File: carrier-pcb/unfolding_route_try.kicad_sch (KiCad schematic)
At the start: 71 parts, among them J1 USB4125-GF-A_REVA, J2 Conn_01x01_Female, J3 1-338068-8, J4 Conn_01x01_Female, J5 Conn_01x01_Female, J6 Conn_01x01_Female, U1 TCA9548APWR, U10 DRV2605LDGS, U11 DRV2605LDGS, U12 BMX160, U13 USBLC6-2SC6, U2 TCA9548APWR, U3 DRV2605LDGS, U4 DRV2605LDGS, U5 DRV2605LDGS, U6 DRV2605LDGS, U7 DRV2605LDGS, U8 DRV2605LDGS, U9 DRV2605LDGS

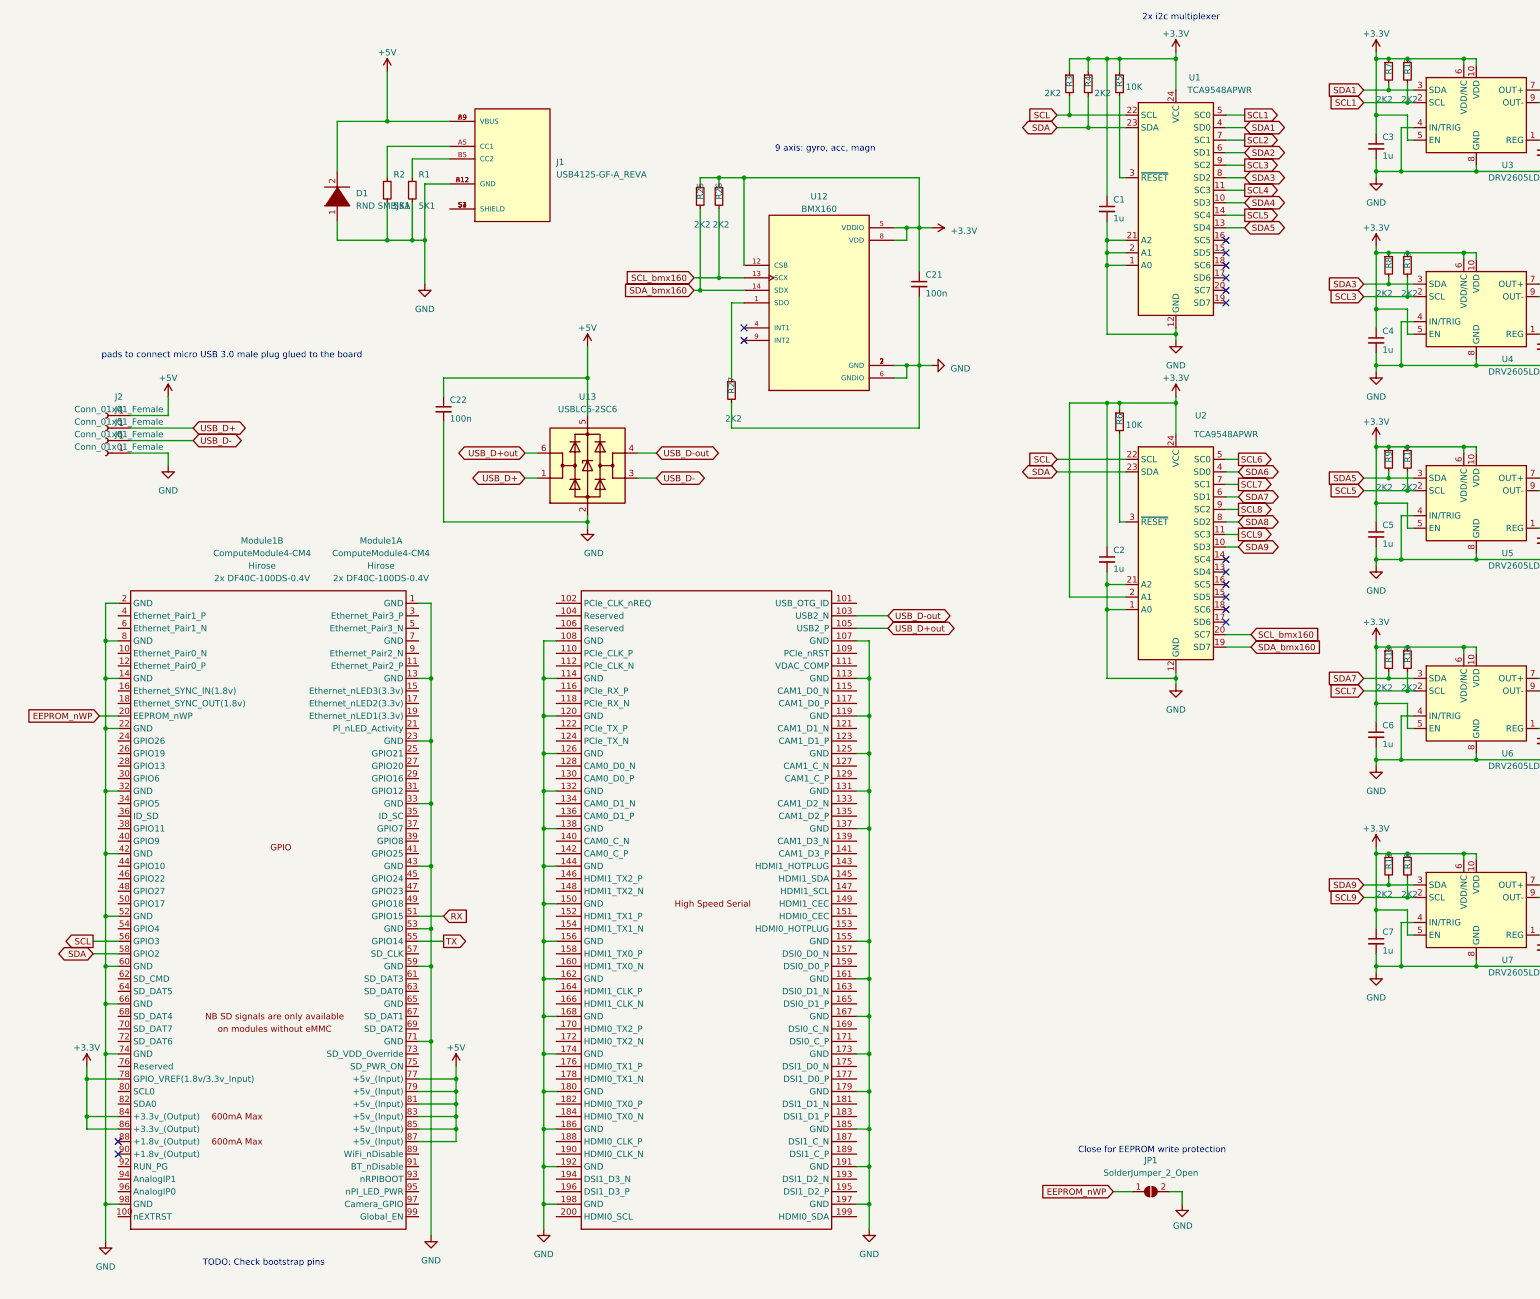
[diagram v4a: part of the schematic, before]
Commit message: Added compass, added LEDs, changed USB TVS diode, fixed power TVS diode direction, moved accelerometer, misc minor improvements
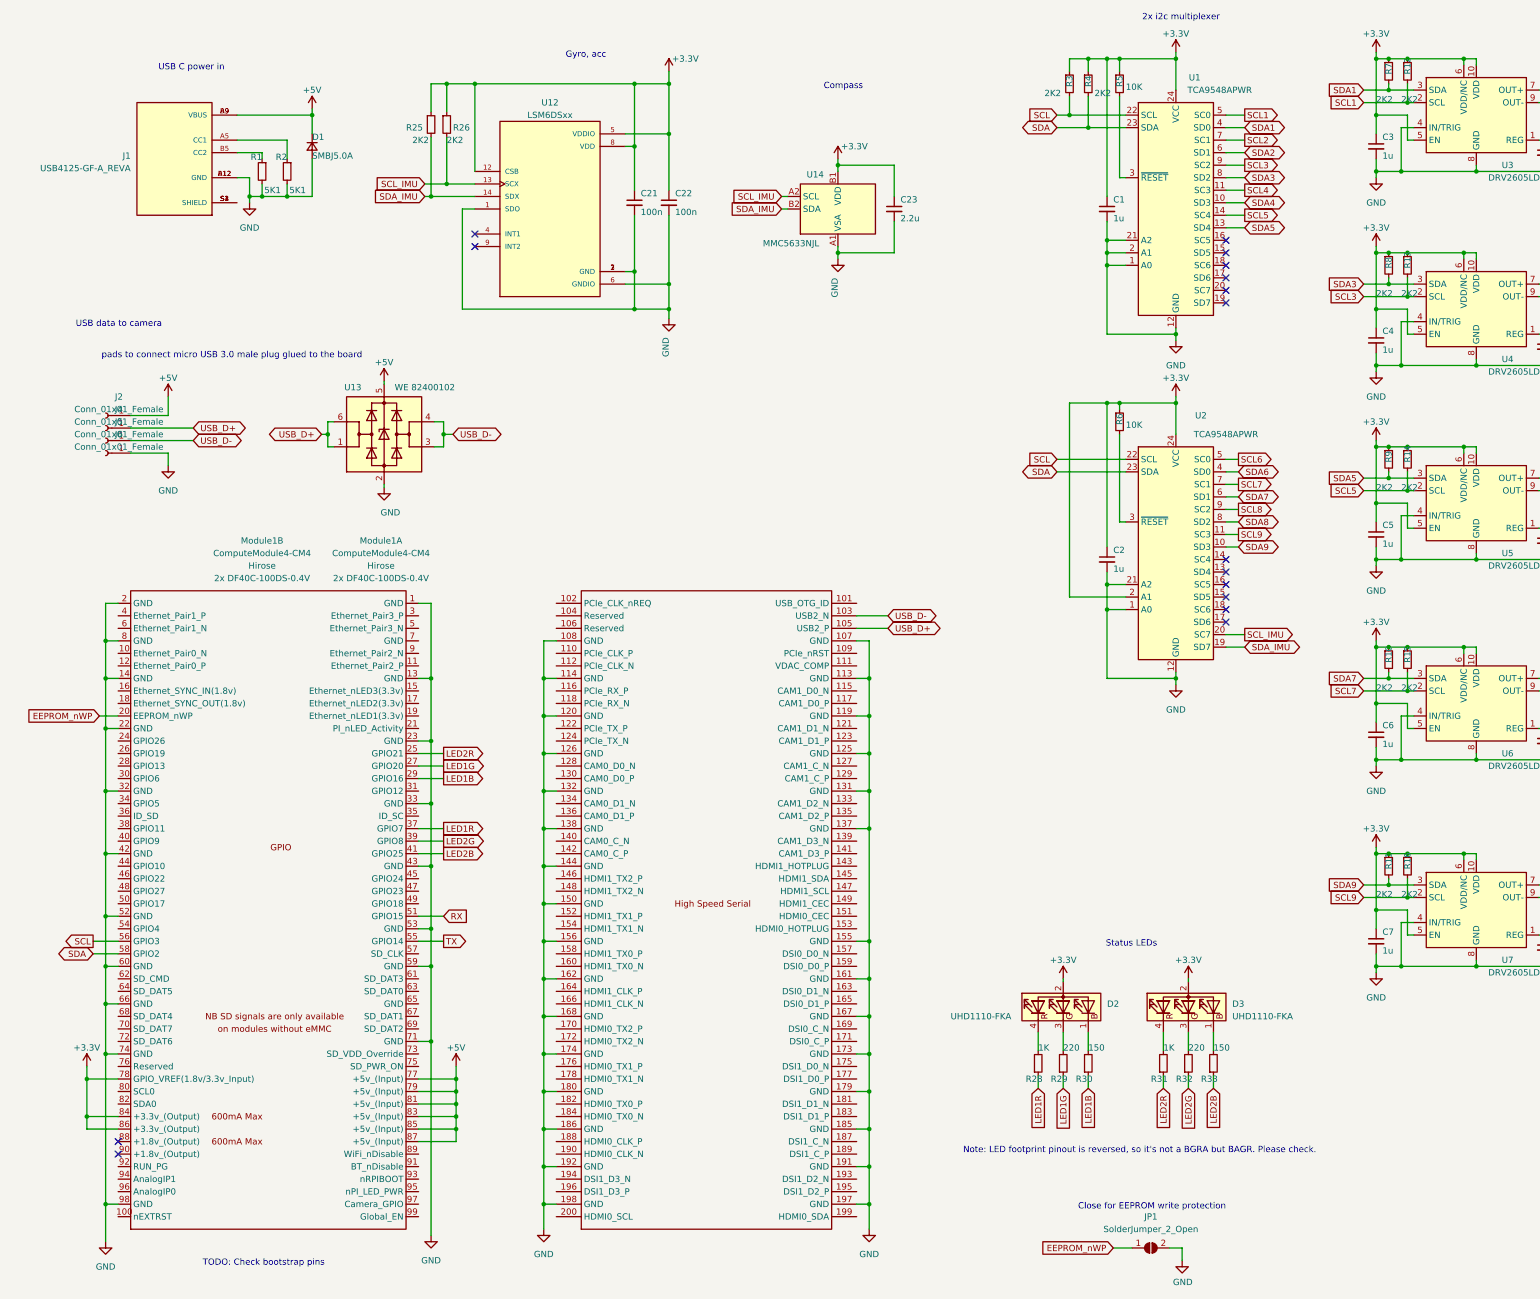
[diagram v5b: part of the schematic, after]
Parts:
- removed D1: RND SMBJ5A, Diode_SMD:D_SMA, symbol pspice:DIODE
- removed R27: 2K2, Resistor_SMD:R_0603_1608Metric, symbol Device:R_Small
- added C23: 2.2u, Capacitor_SMD:C_0603_1608Metric, symbol Device:C_Small
- added D1: SMBJ5.0A, Diode_SMD:D_SMA, symbol Device:D_Small
- added D2, D3: UHD1110-FKA, LED_SMD:LED_Lumex_SML-LX0404SIUPGUSB, symbol Device:LED_BAGR
- added R28, R31: 1K, Resistor_SMD:R_0603_1608Metric, symbol Device:R_Small
- added R29, R32: 220, Resistor_SMD:R_0603_1608Metric, symbol Device:R_Small
- added R30, R33: 150, Resistor_SMD:R_0603_1608Metric, symbol Device:R_Small
- added U14: MMC5633NJL, Package_BGA:WLP-4_0.86x0.86mm_P0.4mm, symbol Sensor_Magnetic:MMC5633NJL
- C1: footprint own:CUI_UJC-HP-3-SMT-TR -> Capacitor_SMD:C_0603_1608Metric
- U1, U10, U11, U2, U3, U4, U5, U6, U7, U8, U9: MF (none) -> TI
- U12: value BMX160 -> LSM6DSxx; MF Bosch -> ST Micro
- U13: value USBLC6-2SC6 -> WE 82400102; MF (none) -> Würth Elektronik
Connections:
- net USB_D+out is gone; now on net USB_D+: Module1.105 (USB2_P), U13.6 (I/O1)
- net USB_D-out is gone; now on net USB_D-: Module1.103 (USB2_N), U13.4 (I/O2)
- net +3V3: now also C22.1, C23.1, D2.2 (A), D3.2 (A), U14.B1 (VDD)
- net +5V: now also D1.1 (K); no longer C22.1
- net GND: now also U12.1 (SDO), C23.2, D1.2 (A), U14.A1 (VSA)
- net LED2R: now reaches Module1.25 (GPIO21)
- net LED2R: now also R31.1
- net LED1G: now reaches Module1.27 (GPIO20)
- net LED1G: now also R29.1
- net LED1B: now reaches Module1.29 (GPIO16)
- net LED1B: now also R30.1
- net LED1R: now reaches Module1.37 (GPIO7)
- net LED1R: now also R28.1
- net LED2G: now reaches Module1.39 (GPIO8)
- net LED2G: now also R32.1
- net LED2B: now reaches Module1.41 (GPIO25)
- net LED2B: now also R33.1
- net SCL_bmx160 renamed SCL_IMU
- net SCL_IMU: now also U14.A2 (SCL)
- net SDA_bmx160 renamed SDA_IMU
- net SDA_IMU: now also U14.B2 (SDA)
- new net: D2.1 (BK), R30.2
- new net: D2.4 (RK), R28.2
- new net: D3.1 (BK), R33.2
- new net: D3.3 (GK), R32.2
- new net: D3.4 (RK), R31.2
- new net: D2.3 (GK), R29.2
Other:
- note added: "Compass"
- note added: "Gyro, acc"
- note added: "Note: LED footprint pinout is reversed, so it's not a BGRA but BAGR. Please check."
- note added: "Status LEDs"
- note added: "USB C power in"
- note added: "USB data to camera"
- note removed: "9 axis: gyro, acc, magn"
- moved on the sheet: C21, C22, J1, JP1, R1, R2, R25, R26, U12, U13

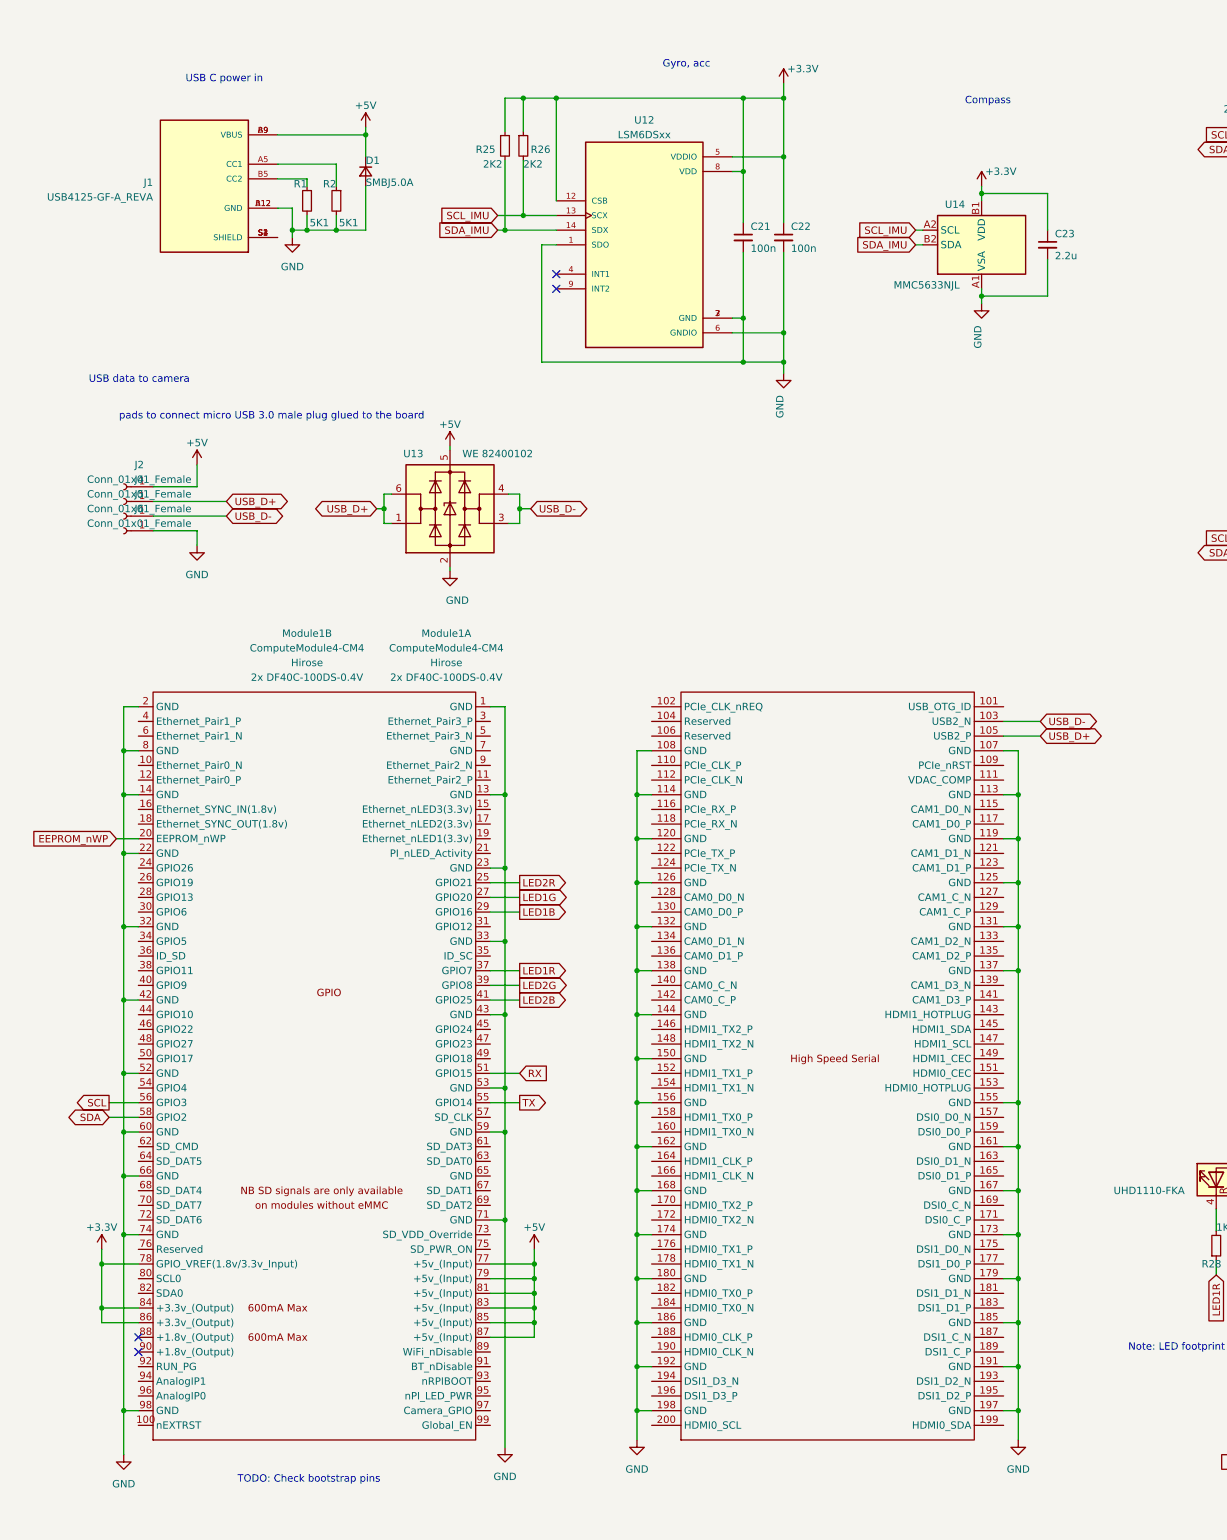
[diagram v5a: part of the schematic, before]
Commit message: Added Pico-SPOX connector for 5V fan
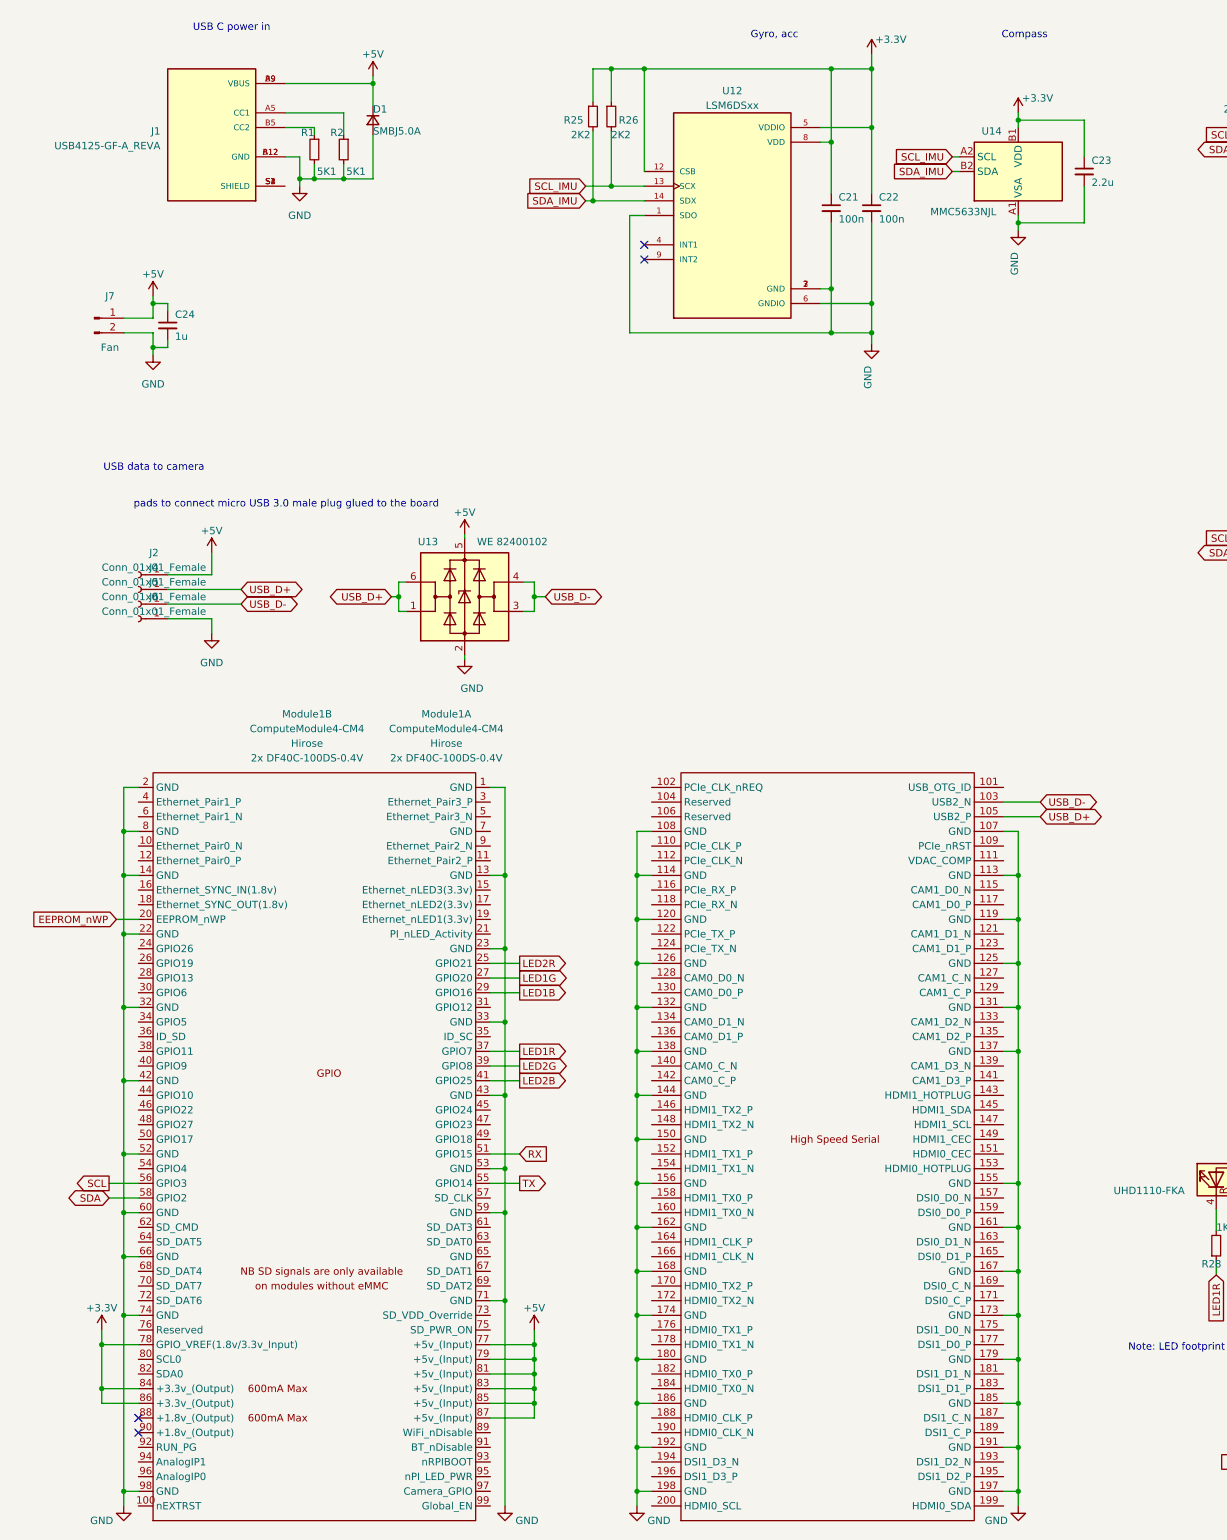
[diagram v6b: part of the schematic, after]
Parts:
- added C24: 1u, Capacitor_SMD:C_0603_1608Metric, symbol Device:C_Small
- added J7: Fan, Pico-Spox:PICOspox-2-v, symbol Connector:Conn_01x02_Male
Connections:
- net +5V: now also C24.1, J7.1 (Pin_1)
- net GND: now also C24.2, J7.2 (Pin_2)
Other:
- note removed: "TODO: Check bootstrap pins"
- moved on the sheet: C21, C22, C23, D1, J1, J2, J4, J5, J6, Module1A, Module1B, R1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
